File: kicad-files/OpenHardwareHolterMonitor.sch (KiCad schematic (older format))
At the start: 11 parts

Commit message: added micro-USB and isolated power
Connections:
- net labels added: Bat1charging, Bat2Charging, Vbat1, Vbat2
- wire segments 95 -> 103
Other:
- moved on the sheet: Q?, R?
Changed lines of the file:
@@
 LIBS:mcp73833
 LIBS:lp5912
+LIBS:rem_3-xxxxs
 LIBS:OpenHardwareHolterMonitor-cache
 EELAYER 25 0
@@
 L S8050 Q?
 U 1 1 5A2C0790
-P 5200 4850
-F 0 "Q?" H 5400 4925 50  0000 L CNN
-F 1 "S8050" H 5400 4850 50  0000 L CNN
-F 2 "TO-92" H 5400 4775 50  0000 L CIN
-F 3 "" H 5200 4850 50  0000 L CNN
-	1    5200 4850
+P 4800 4850
+F 0 "Q?" H 5000 4925 50  0000 L CNN
+F 1 "S8050" H 5000 4850 50  0000 L CNN
+F 2 "TO-92" H 5000 4775 50  0000 L CIN
+F 3 "" H 4800 4850 50  0000 L CNN
+	1    4800 4850
 	1    0    0    -1
 $EndComp
@@
 L S8050 Q?
 U 1 1 5A2C0855
-P 5200 5600
-F 0 "Q?" H 5400 5675 50  0000 L CNN
-F 1 "S8050" H 5400 5600 50  0000 L CNN
-F 2 "TO-92" H 5400 5525 50  0000 L CIN
-F 3 "" H 5200 5600 50  0000 L CNN
-	1    5200 5600
+P 4800 5600
+F 0 "Q?" H 5000 5675 50  0000 L CNN
+F 1 "S8050" H 5000 5600 50  0000 L CNN
+F 2 "TO-92" H 5000 5525 50  0000 L CIN
+F 3 "" H 4800 5600 50  0000 L CNN
+	1    4800 5600
 	1    0    0    1
 $EndComp
@@
 L R R?
 U 1 1 5A2C0A57
-P 4750 4850
-F 0 "R?" V 4830 4850 50  0000 C CNN
-F 1 "12K" V 4750 4850 50  0000 C CNN
-F 2 "" V 4680 4850 50  0000 C CNN
-F 3 "" H 4750 4850 50  0000 C CNN
-	1    4750 4850
+P 4350 4850
+F 0 "R?" V 4430 4850 50  0000 C CNN
+F 1 "12K" V 4350 4850 50  0000 C CNN
+F 2 "" V 4280 4850 50  0000 C CNN
+F 3 "" H 4350 4850 50  0000 C CNN
+	1    4350 4850
 	0    1    1    0
 $EndComp
@@
 L R R?
 U 1 1 5A2C0ACC
-P 4750 5600
-F 0 "R?" V 4830 5600 50  0000 C CNN
-F 1 "12K" V 4750 5600 50  0000 C CNN
-F 2 "" V 4680 5600 50  0000 C CNN
-F 3 "" H 4750 5600 50  0000 C CNN
-	1    4750 5600
-	0    1    1    0
-$EndComp
-Wire Wire Line
-	4900 4850 5000 4850
-Wire Wire Line
-	4900 5600 5000 5600
-Wire Wire Line
-	4300 4850 4600 4850
-Wire Wire Line
-	4300 5600 4600 5600
-Wire Wire Line
-	4550 5600 4550 5150
-Wire Wire Line
-	4550 5150 5300 5150
-Wire Wire Line
-	5300 5150 5300 5050
-Connection ~ 4550 5600
-Wire Wire Line
-	4450 4850 4450 5250
-Wire Wire Line
-	4450 5250 5300 5250
-Wire Wire Line
-	5300 5250 5300 5400
-Connection ~ 4450 4850
-Text Label 4300 4850 0    60   ~ 0
+P 4350 5600
+F 0 "R?" V 4430 5600 50  0000 C CNN
+F 1 "12K" V 4350 5600 50  0000 C CNN
+F 2 "" V 4280 5600 50  0000 C CNN
+F 3 "" H 4350 5600 50  0000 C CNN
+	1    4350 5600
+	0    1    1    0
+$EndComp
+Wire Wire Line
+	4500 4850 4600 4850
+Wire Wire Line
+	4500 5600 4600 5600
+Wire Wire Line
+	3900 4850 4200 4850
+Wire Wire Line
+	3900 5600 4200 5600
+Wire Wire Line
+	4150 5600 4150 5150
+Wire Wire Line
+	4150 5150 4900 5150
+Wire Wire Line
+	4900 5150 4900 5050
+Connection ~ 4150 5600
+Wire Wire Line
+	4050 4850 4050 5250
+Wire Wire Line
+	4050 5250 4900 5250
+Wire Wire Line
+	4900 5250 4900 5400
+Connection ~ 4050 4850
+Text Label 3900 4850 0    60   ~ 0
 DTR
-Text Label 4300 5600 0    60   ~ 0
+Text Label 3900 5600 0    60   ~ 0
 RTS
 Wire Wire Line
-	5300 4650 5300 4600
-Wire Wire Line
-	5300 4600 5650 4600
-Wire Wire Line
-	5300 5800 5300 5900
-Wire Wire Line
-	5300 5900 5650 5900
-Text Label 5650 5900 2    60   ~ 0
+	4900 4650 4900 4600
+Wire Wire Line
+	4900 4600 5250 4600
+Wire Wire Line
+	4900 5800 4900 5900
+Wire Wire Line
+	4900 5900 5250 5900
+Text Label 5250 5900 2    60   ~ 0
 IO0
-Text Label 5650 4600 2    60   ~ 0
+Text Label 5250 4600 2    60   ~ 0
 EN
-Text Notes 4400 4600 0    30   ~ 0
+Text Notes 4000 4600 0    30   ~ 0
 copied from esp32_core_board_v2 schematic
 $Comp
@@
 F0 "power" 60
 F1 "power.sch" 60
+F2 "Vout_3v3" I L 6200 3800 60
+F3 "Vgnd" I L 6200 3950 60
+F4 "Vbat1" I L 6200 4100 60
+F5 "Vbat2" I L 6200 4250 60
+F6 "~Bat1charging~" I L 6200 4400 60
+F7 "~Bat2Charging~" I L 6200 4550 60
 $EndSheet
+Wire Wire Line
+	5700 3800 6200 3800
+Wire Wire Line
+	5700 3800 5700 3700
+$Comp
+L +3V3 #PWR?
+U 1 1 5AAE0E01
+P 5700 3700
+F 0 "#PWR?" H 5700 3550 50  0001 C CNN
+F 1 "+3V3" H 5700 3840 50  0000 C CNN
+F 2 "" H 5700 3700 50  0000 C CNN
+F 3 "" H 5700 3700 50  0000 C CNN
+	1    5700 3700
+	1    0    0    -1
+$EndComp
+Wire Wire Line
+	6200 3950 5700 3950
+Wire Wire Line
+	5700 3950 5700 4050
+$Comp
+L GND #PWR?
+U 1 1 5AAE0F82
+P 5700 4050
+F 0 "#PWR?" H 5700 3800 50  0001 C CNN
+F 1 "GND" H 5700 3900 50  0000 C CNN
+F 2 "" H 5700 4050 50  0000 C CNN
+F 3 "" H 5700 4050 50  0000 C CNN
+	1    5700 4050
+	1    0    0    -1
+$EndComp
+Wire Wire Line
+	6200 4100 5850 4100
+Text Label 5850 4100 0    60   ~ 0
+Vbat1
+Wire Wire Line
+	6200 4250 5850 4250
+Text Label 5850 4250 0    60   ~ 0
+Vbat2
+Wire Wire Line
+	5500 4550 6200 4550
+Text Label 5500 4550 0    60   ~ 0
+Bat2Charging
+Wire Wire Line
+	6200 4400 5500 4400
+Text Label 5500 4400 0    60   ~ 0
+Bat1charging
 $EndSCHEMATC

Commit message: schematic first draft
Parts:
- added C? (x2): 12pF, symbol C
- added D?: D_Schottky, symbol D_Schottky
- added P?: CONN_01X10, symbol CONN_01X10
- added Q? (x2): Q_NMOS_DGS, symbol Q_NMOS_DGS
- added R? (x2): 3.9k, symbol R
- added R? (x2): 1k, symbol R
- added R? (x2): 100k, symbol R
- added Y?: 32768Hz, symbol Crystal
- P?: value FTDI -> Custom_FTDI; symbol CONN_01X06 -> CONN_01X07
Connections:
- net labels added: CTS, Enable_vbat_read, FTDI_V, IO12, IO14, IO15, IO26, IO27, IO36, IO39, IO4, RTC_N, RTC_P, read_bat_1, read_bat_2
- net labels removed: DTR?_CTS?, PWR?
- wire segments 103 -> 157
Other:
- note added: "FK161"
- note removed: "do we want to support power-from-usb while\nprogramming for our porotype?"

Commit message: add vbat to header, and optional power LED
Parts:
- removed P?: CONN_01X10, symbol CONN_01X10
- added P?: CONN_01X12, symbol CONN_01X12
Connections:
- wire segments 157 -> 159
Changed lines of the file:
@@
 Wire Wire Line
 	10200 2300 9900 2300
-$Comp
-L CONN_01X10 P?
-U 1 1 5AB8C674
-P 10400 2550
-F 0 "P?" H 10400 3100 50  0000 C CNN
-F 1 "CONN_01X10" V 10500 2550 50  0000 C CNN
-F 2 "" H 10400 2550 50  0000 C CNN
-F 3 "" H 10400 2550 50  0000 C CNN
-	1    10400 2550
-	1    0    0    -1
-$EndComp
 Wire Wire Line
 	10200 2200 9900 2200
@@
 Text Label 4800 6350 0    60   ~ 0
 DTR
+$Comp
+L CONN_01X12 P?
+U 1 1 5AB69982
+P 10400 2650
+F 0 "P?" H 10400 3300 50  0000 C CNN
+F 1 "CONN_01X12" V 10500 2650 50  0000 C CNN
+F 2 "" H 10400 2650 50  0000 C CNN
+F 3 "" H 10400 2650 50  0000 C CNN
+	1    10400 2650
+	1    0    0    -1
+$EndComp
+Wire Wire Line
+	10200 3100 9900 3100
+Wire Wire Line
+	10200 3200 9900 3200
+Text Label 9900 3100 0    60   ~ 0
+Vbat1
+Text Label 9900 3200 0    60   ~ 0
+Vbat2
 $EndSCHEMATC

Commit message: multiplex power-in
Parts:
- removed P?: CONN_01X12, symbol CONN_01X12
- added J?: Conn_01x13, symbol Conn_01x13
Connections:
- net labels added: IO13
- wire segments 159 -> 162
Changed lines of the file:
@@
 LIBS:rem_3-xxxxs
 LIBS:switches
+LIBS:tps2113a
 LIBS:OpenHardwareHolterMonitor-cache
 EELAYER 25 0
@@
 Wire Wire Line
 	1400 3200 1100 3200
-Text Label 9900 2700 0    60   ~ 0
+Text Label 9900 2800 0    60   ~ 0
 IO26
-Text Label 9900 2800 0    60   ~ 0
+Text Label 9900 2900 0    60   ~ 0
 IO27
-Text Label 9900 2500 0    60   ~ 0
+Text Label 9900 2600 0    60   ~ 0
 IO14
 Text Label 9900 2400 0    60   ~ 0
 IO12
 Wire Wire Line
-	10200 2700 9900 2700
-Wire Wire Line
 	10200 2800 9900 2800
 Wire Wire Line
-	10200 2500 9900 2500
+	10200 2900 9900 2900
+Wire Wire Line
+	10200 2600 9900 2600
 Wire Wire Line
 	10200 2400 9900 2400
-Wire Wire Line
-	10200 2900 9900 2900
-Text Label 9900 2900 0    60   ~ 0
-IO36
 Wire Wire Line
 	10200 3000 9900 3000
 Text Label 9900 3000 0    60   ~ 0
+IO36
+Wire Wire Line
+	10200 3100 9900 3100
+Text Label 9900 3100 0    60   ~ 0
 IO39
 Text Label 2900 4000 1    60   ~ 0
@@
 Wire Wire Line
 	2900 3700 2900 4000
-Text Label 9900 2600 0    60   ~ 0
+Text Label 9900 2700 0    60   ~ 0
 IO15
 Wire Wire Line
-	10200 2600 9900 2600
+	10200 2700 9900 2700
 Text Label 4000 3100 2    60   ~ 0
 IO4
@@
 Text Label 4800 6350 0    60   ~ 0
 DTR
-$Comp
-L CONN_01X12 P?
-U 1 1 5AB69982
-P 10400 2650
-F 0 "P?" H 10400 3300 50  0000 C CNN
-F 1 "CONN_01X12" V 10500 2650 50  0000 C CNN
-F 2 "" H 10400 2650 50  0000 C CNN
-F 3 "" H 10400 2650 50  0000 C CNN
-	1    10400 2650
-	1    0    0    -1
-$EndComp
-Wire Wire Line
-	10200 3100 9900 3100
 Wire Wire Line
 	10200 3200 9900 3200
-Text Label 9900 3100 0    60   ~ 0
+Wire Wire Line
+	10200 3300 9900 3300
+Text Label 9900 3200 0    60   ~ 0
 Vbat1
-Text Label 9900 3200 0    60   ~ 0
+Text Label 9900 3300 0    60   ~ 0
 Vbat2
+Wire Wire Line
+	2200 3700 2200 3900
+Wire Wire Line
+	2200 3900 1650 3900
+Text Label 1650 3900 0    60   ~ 0
+IO13
+$Comp
+L Conn_01x13 J?
+U 1 1 5B0E264F
+P 10400 2700
+F 0 "J?" H 10400 3400 50  0000 C CNN
+F 1 "Conn_01x13" H 10400 2000 50  0000 C CNN
+F 2 "" H 10400 2700 50  0001 C CNN
+F 3 "" H 10400 2700 50  0001 C CNN
+	1    10400 2700
+	1    0    0    -1
+$EndComp
+Wire Wire Line
+	10200 2500 9900 2500
+Text Label 9900 2500 0    60   ~ 0
+IO13
 $EndSCHEMATC

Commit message: fix rules-check issues
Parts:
- removed J?: Conn_01x13, symbol Conn_01x13
- added J1: Conn_01x14, symbol Conn_01x14
- gave numbers to parts that had none: 23
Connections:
- net +3V3: now also J1.2 (Pin_2)
- net GND: now also J1.1 (Pin_1)
- net IO12: now also J1.5 (Pin_5)
- net IO13: now also J1.6 (Pin_6)
- net IO14: now also J1.7 (Pin_7)
- net IO15: now also J1.8 (Pin_8)
- net IO2: now also J1.3 (Pin_3)
- net IO26: now also J1.9 (Pin_9)
- net IO27: now also J1.10 (Pin_10)
- net IO36: now also J1.11 (Pin_11)
- net IO39: now also J1.12 (Pin_12)
- net IO4: now also J1.4 (Pin_4)
- net Vbat1: now also J1.13 (Pin_13)
- net Vbat2: now also J1.14 (Pin_14)
- no-connect marks 0 -> 1
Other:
- note added: "TODO - Custom FTDI?"

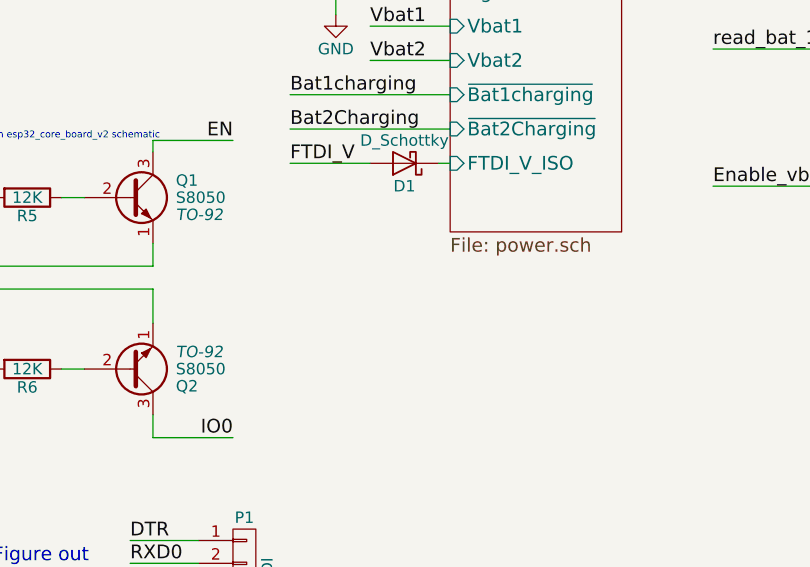
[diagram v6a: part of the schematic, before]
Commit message: assign some footprints
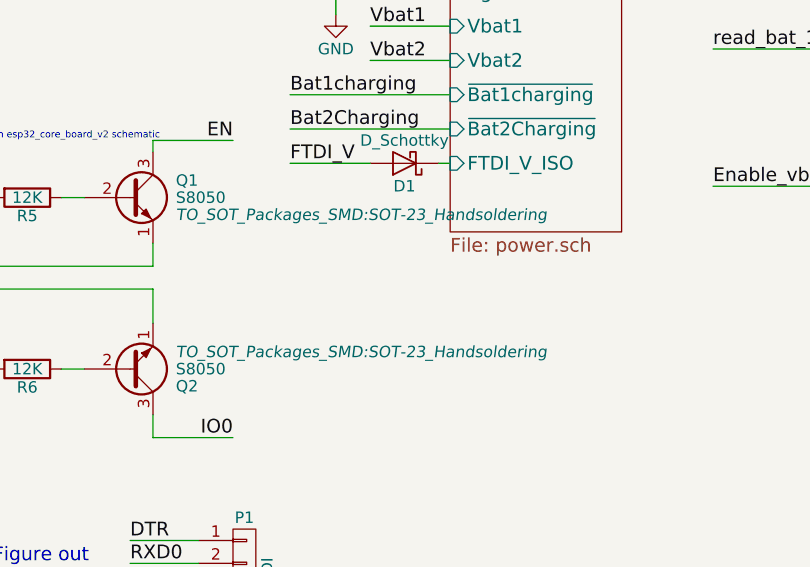
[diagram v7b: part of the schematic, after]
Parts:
- C1, C2: footprint (none) -> Capacitors_SMD:C_0603_HandSoldering
- CON1: footprint (none) -> Connectors_Card:MicroSd_Wurth_693072010801
- D1: footprint (none) -> Diodes_SMD:D_SOD-323_HandSoldering
- J1: footprint (none) -> Pin_Headers:Pin_Header_Straight_1x14_Pitch2.54mm
- P1: footprint (none) -> Pin_Headers:Pin_Header_Straight_1x07_Pitch2.54mm
- Q1, Q2: footprint TO-92 -> TO_SOT_Packages_SMD:SOT-23_Handsoldering
- Q3, Q4: footprint (none) -> TO_SOT_Packages_SMD:SOT-23W_Handsoldering
- R1, R10, R11, R12, R2, R3, R4, R5, R6, R7, R8, R9: footprint (none) -> Resistors_SMD:R_0603_HandSoldering
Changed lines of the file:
@@
 F 0 "CON1" H 1850 6200 50  0000 C CNN
 F 1 "Micro_SD_Card" H 3150 6200 50  0000 R CNN
-F 2 "" H 3650 5900 50  0000 C CNN
+F 2 "Connectors_Card:MicroSd_Wurth_693072010801" H 3650 5900 50  0001 C CNN
 F 3 "" H 2500 5600 50  0000 C CNN
 	1    2500 5600
@@
 F 0 "Q1" H 5000 4925 50  0000 L CNN
 F 1 "S8050" H 5000 4850 50  0000 L CNN
-F 2 "TO-92" H 5000 4775 50  0000 L CIN
+F 2 "TO_SOT_Packages_SMD:SOT-23_Handsoldering" H 5000 4775 50  0000 L CIN
 F 3 "" H 4800 4850 50  0000 L CNN
 	1    4800 4850
@@
 F 0 "Q2" H 5000 5675 50  0000 L CNN
 F 1 "S8050" H 5000 5600 50  0000 L CNN
-F 2 "TO-92" H 5000 5525 50  0000 L CIN
+F 2 "TO_SOT_Packages_SMD:SOT-23_Handsoldering" H 5000 5525 50  0000 L CIN
 F 3 "" H 4800 5600 50  0000 L CNN
 	1    4800 5600
@@
 F 0 "R5" V 4430 4850 50  0000 C CNN
 F 1 "12K" V 4350 4850 50  0000 C CNN
-F 2 "" V 4280 4850 50  0000 C CNN
+F 2 "Resistors_SMD:R_0603_HandSoldering" V 4280 4850 50  0001 C CNN
 F 3 "" H 4350 4850 50  0000 C CNN
 	1    4350 4850
@@
 F 0 "R6" V 4430 5600 50  0000 C CNN
 F 1 "12K" V 4350 5600 50  0000 C CNN
-F 2 "" V 4280 5600 50  0000 C CNN
+F 2 "Resistors_SMD:R_0603_HandSoldering" V 4280 5600 50  0001 C CNN
 F 3 "" H 4350 5600 50  0000 C CNN
 	1    4350 5600
@@
 F 0 "P1" H 5300 7050 50  0000 C CNN
 F 1 "Custom_FTDI" V 5400 6650 50  0000 C CNN
-F 2 "" H 5300 6650 50  0000 C CNN
+F 2 "Pin_Headers:Pin_Header_Straight_1x07_Pitch2.54mm" H 5300 6650 50  0001 C CNN
 F 3 "" H 5300 6650 50  0000 C CNN
 	1    5300 6650
@@
 F 0 "R1" V 4430 2000 50  0000 C CNN
 F 1 "47" V 4350 2000 50  0000 C CNN
-F 2 "" V 4280 2000 50  0000 C CNN
+F 2 "Resistors_SMD:R_0603_HandSoldering" V 4280 2000 50  0001 C CNN
 F 3 "" H 4350 2000 50  0000 C CNN
 	1    4350 2000
@@
 F 0 "R2" V 4430 2700 50  0000 C CNN
 F 1 "47" V 4350 2700 50  0000 C CNN
-F 2 "" V 4280 2700 50  0000 C CNN
+F 2 "Resistors_SMD:R_0603_HandSoldering" V 4280 2700 50  0001 C CNN
 F 3 "" H 4350 2700 50  0000 C CNN
 	1    4350 2700
@@
 F 0 "R3" V 4430 2800 50  0000 C CNN
 F 1 "47" V 4350 2800 50  0000 C CNN
-F 2 "" V 4280 2800 50  0000 C CNN
+F 2 "Resistors_SMD:R_0603_HandSoldering" V 4280 2800 50  0001 C CNN
 F 3 "" H 4350 2800 50  0000 C CNN
 	1    4350 2800
@@
 F 0 "R4" V 4430 2900 50  0000 C CNN
 F 1 "47" V 4350 2900 50  0000 C CNN
-F 2 "" V 4280 2900 50  0000 C CNN
+F 2 "Resistors_SMD:R_0603_HandSoldering" V 4280 2900 50  0001 C CNN
 F 3 "" H 4350 2900 50  0000 C CNN
 	1    4350 2900
@@
 F 0 "R8" V 8530 3950 50  0000 C CNN
 F 1 "3.9k" V 8450 3950 50  0000 C CNN
-F 2 "" V 8380 3950 50  0000 C CNN
+F 2 "Resistors_SMD:R_0603_HandSoldering" V 8380 3950 50  0001 C CNN
 F 3 "" H 8450 3950 50  0000 C CNN
 	1    8450 3950
@@
 F 0 "R9" V 8530 4400 50  0000 C CNN
 F 1 "1k" V 8450 4400 50  0000 C CNN
-F 2 "" V 8380 4400 50  0000 C CNN
+F 2 "Resistors_SMD:R_0603_HandSoldering" V 8380 4400 50  0001 C CNN
 F 3 "" H 8450 4400 50  0000 C CNN
 	1    8450 4400
@@
 F 0 "Q3" H 8550 4850 50  0000 L CNN
 F 1 "Q_NMOS_DGS" H 8550 4750 50  0000 L CNN
-F 2 "" H 8550 4900 50  0000 C CNN
+F 2 "TO_SOT_Packages_SMD:SOT-23W_Handsoldering" H 8550 4900 50  0001 C CNN
 F 3 "" H 8350 4800 50  0000 C CNN
 	1    8350 4800
@@
 F 0 "R11" V 10280 3950 50  0000 C CNN
 F 1 "3.9k" V 10200 3950 50  0000 C CNN
-F 2 "" V 10130 3950 50  0000 C CNN
+F 2 "Resistors_SMD:R_0603_HandSoldering" V 10130 3950 50  0001 C CNN
 F 3 "" H 10200 3950 50  0000 C CNN
 	1    10200 3950
@@
 F 0 "R12" V 10280 4400 50  0000 C CNN
 F 1 "1k" V 10200 4400 50  0000 C CNN
-F 2 "" V 10130 4400 50  0000 C CNN
+F 2 "Resistors_SMD:R_0603_HandSoldering" V 10130 4400 50  0001 C CNN
 F 3 "" H 10200 4400 50  0000 C CNN
 	1    10200 4400
@@
 F 0 "Q4" H 10300 4850 50  0000 L CNN
 F 1 "Q_NMOS_DGS" H 10300 4750 50  0000 L CNN
-F 2 "" H 10300 4900 50  0000 C CNN
+F 2 "TO_SOT_Packages_SMD:SOT-23W_Handsoldering" H 10300 4900 50  0001 C CNN
 F 3 "" H 10100 4800 50  0000 C CNN
 	1    10100 4800
@@
 F 0 "R10" V 9730 5000 50  0000 C CNN
 F 1 "100k" V 9650 5000 50  0000 C CNN
-F 2 "" V 9580 5000 50  0000 C CNN
+F 2 "Resistors_SMD:R_0603_HandSoldering" V 9580 5000 50  0001 C CNN
 F 3 "" H 9650 5000 50  0000 C CNN
 	1    9650 5000
@@
 F 0 "R7" V 7980 5000 50  0000 C CNN
 F 1 "100k" V 7900 5000 50  0000 C CNN
-F 2 "" V 7830 5000 50  0000 C CNN
+F 2 "Resistors_SMD:R_0603_HandSoldering" V 7830 5000 50  0001 C CNN
 F 3 "" H 7900 5000 50  0000 C CNN
 	1    7900 5000
@@
 F 0 "Y1" H 8250 2450 50  0000 C CNN
 F 1 "32768Hz" H 8250 2150 50  0000 C CNN
-F 2 "" H 8250 2300 50  0000 C CNN
+F 2 "" H 8250 2300 50  0001 C CNN
 F 3 "" H 8250 2300 50  0000 C CNN
 	1    8250 2300
@@
 F 0 "C1" H 7975 2850 50  0000 L CNN
 F 1 "12pF" H 7975 2650 50  0000 L CNN
-F 2 "" H 7988 2600 50  0000 C CNN
+F 2 "Capacitors_SMD:C_0603_HandSoldering" H 7988 2600 50  0001 C CNN
 F 3 "" H 7950 2750 50  0000 C CNN
 	1    7950 2750
@@
 F 0 "C2" H 8575 2850 50  0000 L CNN
 F 1 "12pF" H 8575 2650 50  0000 L CNN
-F 2 "" H 8588 2600 50  0000 C CNN
+F 2 "Capacitors_SMD:C_0603_HandSoldering" H 8588 2600 50  0001 C CNN
 F 3 "" H 8550 2750 50  0000 C CNN
 	1    8550 2750
@@
 F 0 "D1" H 6000 4800 50  0000 C CNN
 F 1 "D_Schottky" H 6000 4600 50  0000 C CNN
-F 2 "" H 6000 4700 50  0000 C CNN
+F 2 "Diodes_SMD:D_SOD-323_HandSoldering" H 6000 4700 50  0001 C CNN
 F 3 "" H 6000 4700 50  0000 C CNN
 	1    6000 4700
@@
 F 0 "J1" H 10400 3400 50  0000 C CNN
 F 1 "Conn_01x14" H 10400 1900 50  0000 C CNN
-F 2 "" H 10400 2700 50  0001 C CNN
+F 2 "Pin_Headers:Pin_Header_Straight_1x14_Pitch2.54mm" H 10400 2700 50  0001 C CNN
 F 3 "" H 10400 2700 50  0001 C CNN
 	1    10400 2700
